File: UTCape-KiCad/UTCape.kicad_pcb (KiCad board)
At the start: 2 copper layers, 86.4 x 54.6 mm, 50 parts, among them IC1 74LVC1G157, IC2 EEPROM-25LC-SOT23, IC3 EEPROM-24LC, IC4 EEPROM-24LC, IC5 LM555, J1 BBB_P8, J2 BBB_P9

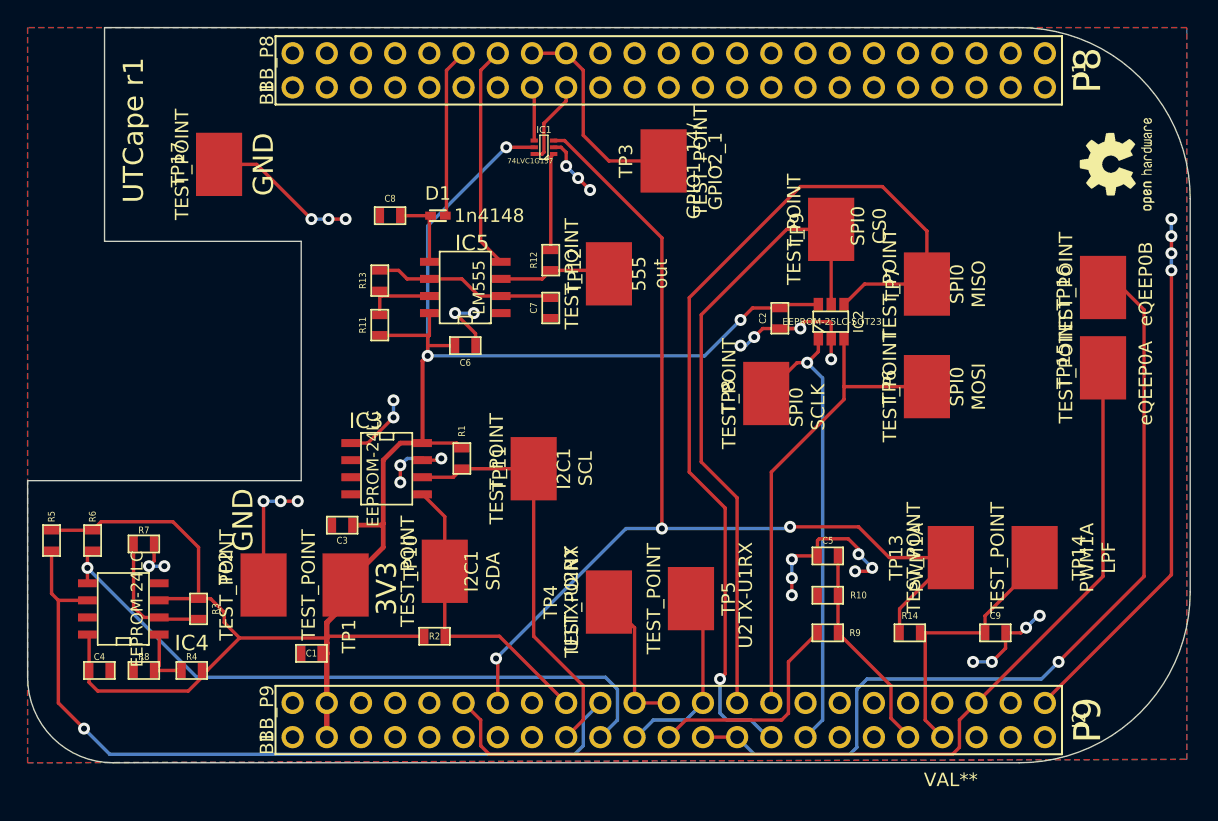
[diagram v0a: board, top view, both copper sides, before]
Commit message: added missing resistor in divider plus some protection resistors, regenerated fab files
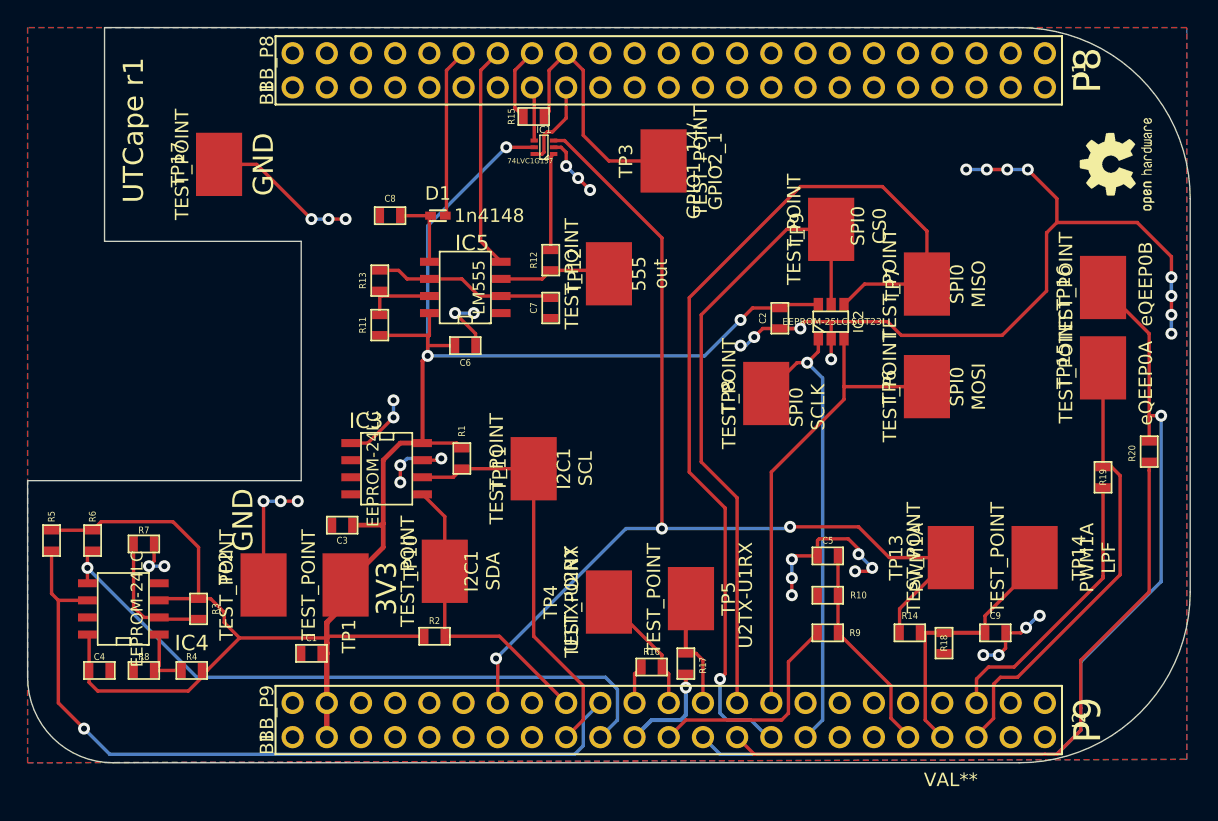
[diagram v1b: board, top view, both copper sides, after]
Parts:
- added R15: 100, SM0603, F.Cu at (205.0, 112.3)
- added R16: 100, SM0603, F.Cu at (213.7, 153.2)
- added R17: 100, SM0603, F.Cu at (216.3, 152.9)
- added R18: 5.6k, SM0603, F.Cu at (235.5, 151.4)
- added R19: 100, SM0603, F.Cu at (247.3, 139.1)
- added R20: 100, SM0603, F.Cu at (250.7, 137.2)
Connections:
- J1 pad 18: /BeagleBone Headers/GPIO1_14 -> /BeagleBone Headers/GPIO2_1
- J2 pad 12: /BeagleBone Headers/GPIO1_28 -> (no net)
- J2 pad 21: /BeagleBone Headers/UART1_RX -> /BeagleBone Headers/UART2_TX
- J2 pad 22: /BeagleBone Headers/UART1_TX -> /BeagleBone Headers/UART2_RX
- J2 pad 27: /BeagleBone Headers/GPIO3_17 -> /BeagleBone Headers/eQEP0_B
- J2 pad 41: (no net) -> /BeagleBone Headers/GPIO0_20
- J2 pad 42: /BeagleBone Headers/GPIO1_28 -> /BeagleBone Headers/eQEP0_A
- TP15 pad 1: /BeagleBone Headers/GPIO1_28 -> /BeagleBone Headers/GPIO0_20
- TP3 pad 1: /BeagleBone Headers/GPIO1_14 -> /BeagleBone Headers/GPIO2_1
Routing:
- net /BeagleBone Headers/GPIO1_28: track 72.3 -> 0.00 mm
- net /BeagleBone Headers/eQEP0_B: track 0.00 -> 48.8 mm
- net /BeagleBone Headers/GPIO0_20: track 0.00 -> 33.5 mm
- net /BeagleBone Headers/eQEP0_A: track 0.00 -> 21.0 mm
- net /BeagleBone Headers/GPIO2_1: track 0.00 -> 18.8 mm
- net /BeagleBone Headers/GPIO1_14: track 15.9 -> 5.49 mm
- net /BeagleBone Headers/UART2_TX: track 0.00 -> 7.54 mm, vias 0 -> 1
- net GND: track 109.7 -> 116.9 mm, vias 34 -> 38
- net /BeagleBone Headers/UART1_RX: track 14.2 -> 8.88 mm
- net /BeagleBone Headers/GPIO3_17: track 64.8 -> 69.3 mm
- net /BeagleBone Headers/UART2_RX: track 0.00 -> 2.88 mm
- net /BeagleBone Headers/UART1_TX: track 10.8 -> 9.33 mm

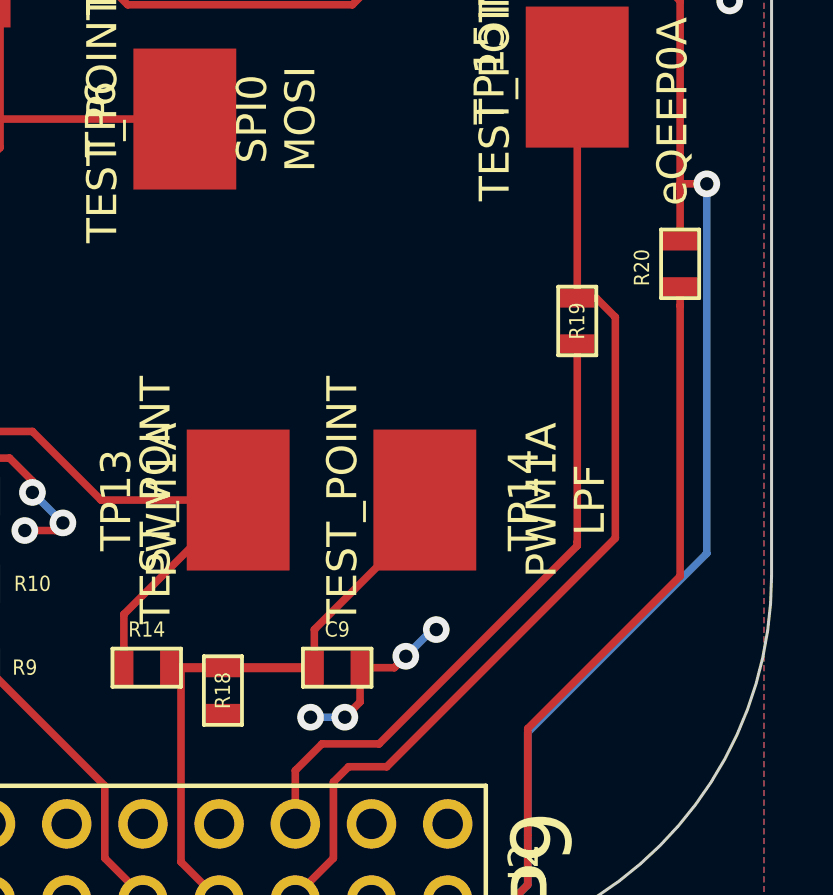
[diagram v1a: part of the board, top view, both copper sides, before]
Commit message: moved some reference designators
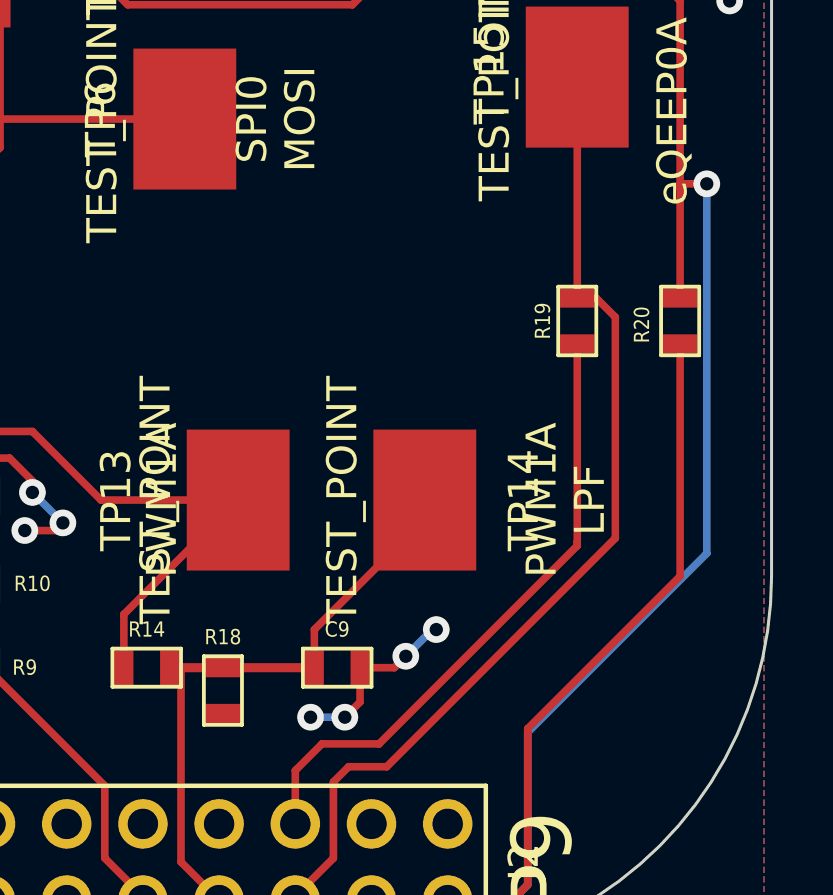
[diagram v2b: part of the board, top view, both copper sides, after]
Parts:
- moved R20 1.91 mm to (250.7, 139.1)
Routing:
- net /BeagleBone Headers/eQEP0_B: track 48.8 -> 46.9 mm
- net /BeagleBone Headers/GPIO3_17: track 69.3 -> 71.2 mm
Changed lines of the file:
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@@
     (links 114)
     (no_connects 0)
-    (area 167.335999 105.613999 253.796001 160.324001)
+    (area 166.9836 105.278267 394.564286 281.87)
     (thickness 1.6)
     (drawings 32)
-    (tracks 387)
+    (tracks 386)
     (zones 0)
     (modules 56)
@@
     (at 235.458 151.384 270)
     (attr smd)
-    (fp_text reference R18 (at 0 0 270) (layer F.SilkS)
+    (fp_text reference R18 (at -1.778 0 360) (layer F.SilkS)
       (effects (font (size 0.508 0.4572) (thickness 0.1143)))
     )
@@
     (at 247.269 139.065 270)
     (attr smd)
-    (fp_text reference R19 (at 0 0 270) (layer F.SilkS)
+    (fp_text reference R19 (at 0 1.143 270) (layer F.SilkS)
       (effects (font (size 0.508 0.4572) (thickness 0.1143)))
     )
@@
   )
   (module SM0603 (layer F.Cu)
-    (at 250.698 137.16 270)
+    (at 250.698 139.065 270)
     (attr smd)
     (fp_text reference R20 (at 0.127 1.27 270) (layer F.SilkS)
@@
   (segment (start 223.393 157.099) (end 223.901 156.591) (width 0.254) (layer F.Cu) (net 2))
   (segment (start 216.281 157.099) (end 223.393 157.099) (width 0.254) (layer F.Cu) (net 2))
-  (segment (start 238.506 150.622) (end 235.458 150.622) (width 0.3048) (layer F.Cu) (net 3))
-  (segment (start 233.68 150.622) (end 235.458 150.622) (width 0.3048) (layer F.Cu) (net 3))
+  (segment (start 238.506 150.622) (end 235.458 150.622) (width 0.3048) (layer F.Cu) (net 3) (status 20))
+  (segment (start 233.68 150.622) (end 235.458 150.622) (width 0.3048) (layer F.Cu) (net 3) (status 20))
   (segment (start 242.189 145.034) (end 242.189 145.669) (width 0.254) (layer F.Cu) (net 3))
   (segment (start 238.506 149.352) (end 238.506 150.622) (width 0.254) (layer F.Cu) (net 3))
@@
   (segment (start 206.121 108.839) (end 206.121 111.887) (width 0.254) (layer F.Cu) (net 9))
   (segment (start 207.391 107.569) (end 208.661 108.839) (width 0.254) (layer F.Cu) (net 9))
+  (segment (start 250.698 138.303) (end 250.698 134.493) (width 0.254) (layer F.Cu) (net 10))
   (segment (start 217.551 158.369) (end 218.821 159.639) (width 0.254) (layer B.Cu) (net 10))
   (segment (start 218.821 159.639) (end 243.84 159.639) (width 0.254) (layer B.Cu) (net 10))
@@
   (segment (start 250.698 134.62) (end 250.698 134.493) (width 0.254) (layer F.Cu) (net 10))
   (segment (start 250.825 134.493) (end 250.698 134.62) (width 0.254) (layer F.Cu) (net 10))
-  (segment (start 250.698 136.398) (end 250.698 134.493) (width 0.254) (layer F.Cu) (net 10))
   (segment (start 250.698 134.493) (end 250.698 128.397) (width 0.254) (layer F.Cu) (net 10))
   (segment (start 250.698 128.397) (end 247.269 124.968) (width 0.254) (layer F.Cu) (net 10))
@@
   (segment (start 237.871 154.051) (end 237.871 155.829) (width 0.254) (layer F.Cu) (net 20))
   (segment (start 247.269 139.827) (end 247.269 146.431) (width 0.254) (layer F.Cu) (net 20))
-  (segment (start 250.698 137.922) (end 250.698 138.557) (width 0.254) (layer F.Cu) (net 21))
-  (segment (start 245.618 156.21) (end 245.618 152.654) (width 0.254) (layer F.Cu) (net 21))
-  (segment (start 221.361 159.639) (end 242.951 159.639) (width 0.254) (layer F.Cu) (net 21))
-  (segment (start 242.951 159.639) (end 243.84 159.639) (width 0.254) (layer F.Cu) (net 21))
-  (segment (start 243.84 159.639) (end 245.618 157.861) (width 0.254) (layer F.Cu) (net 21))
-  (segment (start 245.618 157.861) (end 245.618 156.21) (width 0.254) (layer F.Cu) (net 21))
-  (segment (start 221.361 159.639) (end 220.091 158.369) (width 0.254) (layer F.Cu) (net 21))
-  (segment (start 250.698 147.574) (end 250.698 138.557) (width 0.254) (layer F.Cu) (net 21))
+  (segment (start 250.698 139.827) (end 250.698 147.574) (width 0.254) (layer F.Cu) (net 21))
   (segment (start 245.618 152.654) (end 250.698 147.574) (width 0.254) (layer F.Cu) (net 21))
+  (segment (start 221.361 159.639) (end 220.091 158.369) (width 0.254) (layer F.Cu) (net 21))
+  (segment (start 245.618 157.861) (end 245.618 156.21) (width 0.254) (layer F.Cu) (net 21))
+  (segment (start 243.84 159.639) (end 245.618 157.861) (width 0.254) (layer F.Cu) (net 21))
+  (segment (start 242.951 159.639) (end 243.84 159.639) (width 0.254) (layer F.Cu) (net 21))
+  (segment (start 221.361 159.639) (end 242.951 159.639) (width 0.254) (layer F.Cu) (net 21))
+  (segment (start 245.618 156.21) (end 245.618 152.654) (width 0.254) (layer F.Cu) (net 21))
   (segment (start 169.672 148.209) (end 169.672 155.829) (width 0.254) (layer F.Cu) (net 22))
   (segment (start 208.661 157.099) (end 209.931 155.829) (width 0.254) (layer B.Cu) (net 22))
